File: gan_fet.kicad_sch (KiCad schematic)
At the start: 7 parts, among them J1 Conn_01x04_Male, Q1 EPC2036, U1 NPC81074

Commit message: some misc fiddling with the footprint and a centered model.
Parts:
- C1: value (none) -> 100n; footprint (none) -> Capacitor_SMD:C_1206_3216Metric
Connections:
- net fetGate: now also Q1.1 (S); no longer Q1.3 (G)
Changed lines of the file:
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@@
     (pin "1")
     (pin "2")
-    (pin "3")
+    (pin "1")
     (pin "4")
   )
@@
       (effects (font (size 1.27 1.27)) (justify left))
     )
-    (property "Value" "" (id 1) (at 163.83 91.4399 0)
+    (property "Value" "100n" (id 1) (at 163.83 91.4399 0)
       (effects (font (size 1.27 1.27)) (justify left))
     )
-    (property "Footprint" "" (id 2) (at 160.9852 93.98 0)
+    (property "Footprint" "Capacitor_SMD:C_1206_3216Metric" (id 2) (at 160.9852 93.98 0)
       (effects (font (size 1.27 1.27)) hide)
     )

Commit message: rev_1 board
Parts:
- removed TP1: C_Small, Resistor_SMD:R_1206_3216Metric, symbol Device:C_Small
- added C2: 100n, Capacitor_SMD:C_1206_3216Metric, symbol Device:C
- added C3: 33p, Capacitor_SMD:C_1206_3216Metric, symbol Device:C
- added J2: Driver TestPoint, Connector_Coaxial:SMA_Samtec_SMA-J-P-X-ST-EM1_EdgeMount, symbol Connector:Conn_Coaxial
- added J3: Conn_01x04_Male, Connector_PinHeader_2.54mm:PinHeader_1x04_P2.54mm_Vertical, symbol Connector:Conn_01x04_Male
- added J4: FetGate test point, Connector_Coaxial:SMA_Samtec_SMA-J-P-X-ST-EM1_EdgeMount, symbol Connector:Conn_Coaxial
- added J5, J6: (no value), symbol Connector:Conn_01x01_Male
- added L1: L, Resistor_THT:R_Axial_DIN0204_L3.6mm_D1.6mm_P5.08mm_Horizontal, symbol Device:L
- added R3: 470, Resistor_SMD:R_0805_2012Metric, symbol Device:R_US
- added R5: 470, Resistor_SMD:R_0805_2012Metric_Pad1.20x1.40mm_HandSolder, symbol Device:R_US
- J1: footprint Connector_PinHeader_2.54mm:PinHeader_1x04_P2.54mm_Horizontal -> Connector_PinHeader_2.54mm:PinHeader_1x04_P2.54mm_Vertical
- Q1: symbol Device:Q_NMOS_SDGD -> gan_fet:Q_NMOS_GSDS
- R1: value 1 -> 2.2
- R2: value 4.7 -> 2.2
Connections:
- net GND: now also Q1.2 (S), Q1.4 (Source), C3.2, J2.2 (Ext), J3.3 (Pin_3), J3.4 (Pin_4), J4.2 (Ext), J5.1 (Pin_1), J6.1 (Pin_1); no longer Q1.1 (S)
- net fetGate: now also R5.2
- net gate: now also C2.2, R3.2; no longer U1.1 (IN+)
- removed net drain: J1.3 (Pin_3), Q1.2 (D), Q1.4 (D)
- new net: J2.1 (In), R3.1
- new net: J4.1 (In), R5.1
- new net: C3.1, L1.2, Q1.3 (D)
- new net Vcc: J3.1 (Pin_1), J3.2 (Pin_2), L1.1
- new net driveBias: C2.1, J1.3 (Pin_3), U1.1 (IN+)
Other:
- note added: "470R gives ~10x attenuation 1k gives ~21x"
- note added: "solder braid and center conductor to resistor pads for Zo probe"
- moved on the sheet: C1, J1

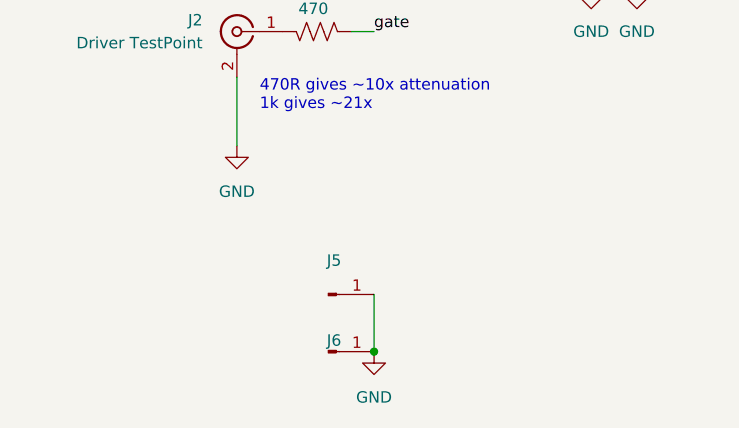
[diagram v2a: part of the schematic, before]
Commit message: add some labels to schematic
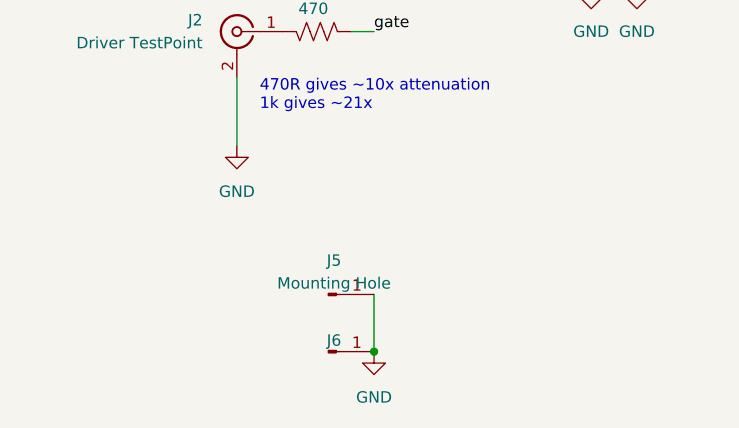
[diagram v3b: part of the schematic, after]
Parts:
- J5: value (none) -> Mounting Hole
- J6: value (none) -> Conn_01x01_Male
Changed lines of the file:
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@@
     (in_bom yes) (on_board yes) (fields_autoplaced)
     (property "Reference" "J5" (id 0) (at 66.675 133.384 0))
-    (property "Value" "" (id 1) (at 66.675 135.9209 0))
+    (property "Value" "Mounting Hole" (id 1) (at 66.675 135.9209 0))
     (property "Footprint" "" (id 2) (at 66.04 137.16 0)
       (effects (font (size 1.27 1.27)) hide)
@@
     (in_bom yes) (on_board yes) (fields_autoplaced)
     (property "Reference" "J6" (id 0) (at 66.675 142.271 0))
-    (property "Value" "" (id 1) (at 66.675 142.2709 0)
+    (property "Value" "Conn_01x01_Male" (id 1) (at 66.675 142.2709 0)
       (effects (font (size 1.27 1.27)) hide)
     )
